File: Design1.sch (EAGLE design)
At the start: 24 parts, among them U1 ATMEGA328P-AU, X1 +3.3

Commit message: update
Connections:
- net ESP12F(PIN21) renamed RX
- net ESP12F(PIN22) renamed TX
- net N$5 renamed CH_PD
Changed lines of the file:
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@@
 <?xml version="1.0" encoding="utf-8"?>
 <!DOCTYPE eagle SYSTEM "eagle.dtd">
-<eagle version="8.5.2">
+<eagle version="8.7.1">
 <drawing>
 <settings>
@@
 </segment>
 </net>
-<net name="ESP12F(PIN21)" class="0">
+<net name="RX" class="0">
 <segment>
 <pinref part="SJ2" gate="1" pin="1"/>
@@
 <pinref part="U1" gate="A" pin="PD1"/>
 <wire x1="342.9" y1="220.98" x2="302.26" y2="220.98" width="0.1524" layer="91"/>
-</segment>
-</net>
-<net name="ESP12F(PIN22)" class="0">
+<label x="358.14" y="167.64" size="1.778" layer="95"/>
+</segment>
+</net>
+<net name="TX" class="0">
 <segment>
 <wire x1="340.36" y1="238.76" x2="340.36" y2="223.52" width="0.1524" layer="91"/>
@@
 <pinref part="MCU_FIRM2" gate="FIRM_PADS" pin="3"/>
 <wire x1="345.44" y1="170.18" x2="342.9" y2="170.18" width="0.1524" layer="91"/>
+<label x="347.98" y="170.18" size="1.778" layer="95"/>
 </segment>
 </net>
@@
 </segment>
 </net>
-<net name="N$5" class="0">
+<net name="CH_PD" class="0">
 <segment>
 <pinref part="U2" gate="G$1" pin="CH_PD"/>
 <wire x1="391.16" y1="233.68" x2="388.62" y2="233.68" width="0.1524" layer="91"/>
-<wire x1="401.32" y1="236.22" x2="391.16" y2="236.22" width="0.1524" layer="91"/>
-<wire x1="391.16" y1="236.22" x2="391.16" y2="233.68" width="0.1524" layer="91"/>
-</segment>
-</net>
+<label x="393.7" y="233.68" size="1.778" layer="95"/>
+</segment>
+</net>

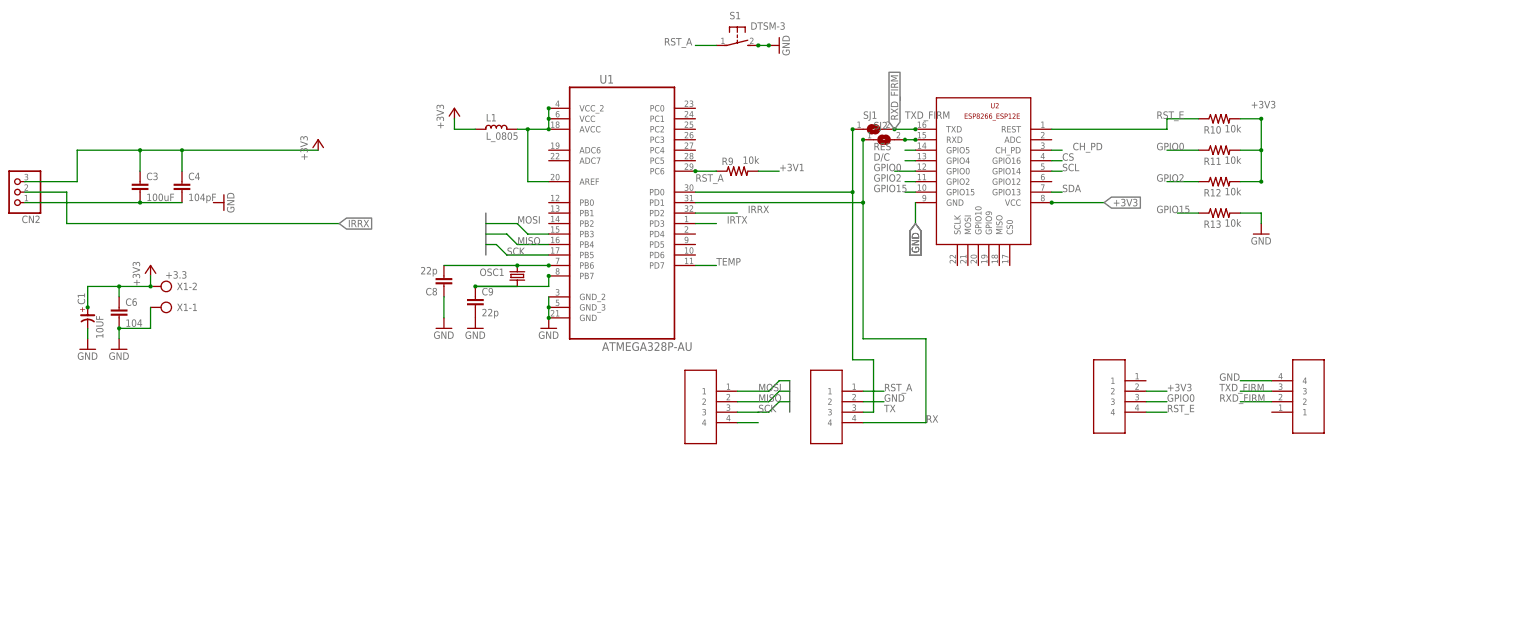
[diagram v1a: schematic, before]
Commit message: v 0.3 needs location buttons only
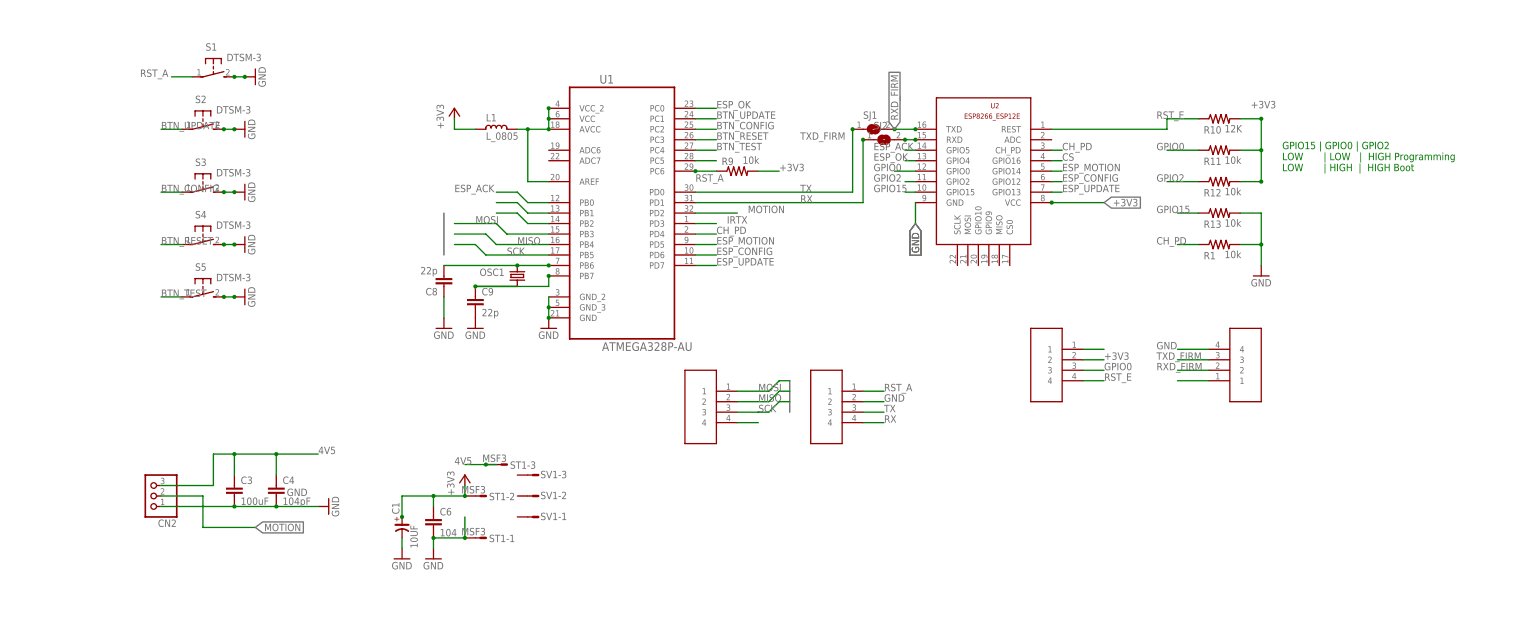
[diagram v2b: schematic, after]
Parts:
- removed X1: +3.3, con-ptr500:AK300/2
- added R1: 10k, SMD Resistors:0.75OHM-1/4W-1%(0805)
- added S2, S3, S4, S5: DTSM-3, switch-tact:DTSM-3
- added ST1: MSF3, con-lumberg:MSF3
- added SV1: (no value), con-amp-mt6:MT6-3Y
- R10: value 10k -> 12K
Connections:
- net IRRX renamed MOTION
- removed net +3V1: R9.2
- removed net D/C: U2.GPIO4
- removed net N$2: C3.2, C4.2, CN2.1
- removed net RES: U2.GPIO5
- removed net SCL: U2.GPIO14
- removed net SDA: U2.GPIO13
- removed net TEMP: U1.PD7
- new net 4V5: C3.1, C4.1, CN2.3, ST1-3.S
- new net BTN_CONFIG: S3.1, U1.PC2
- new net BTN_RESET: S4.1, U1.PC3
- new net BTN_TEST: S5.1, U1.PC4
- new net BTN_UPDATE: S2.1, U1.PC1
- new net ESP_ACK: U1.PB0, U2.GPIO5
- new net ESP_CONFIG: U1.PD6, U2.GPIO12
- new net ESP_MOTION: U1.PD5, U2.GPIO14
- new net ESP_OK: U1.PC0, U2.GPIO4
- new net ESP_UPDATE: U1.PD7, U2.GPIO13
- new net N$1: MCU_FIRM3.1
- new net N$18: U1.PC5
- new net N$4: U$3.1
- new net N$8: U1.PB1
- new net N$9: U1.PB2
- net +3V3: now also R9.2, ST1-2.S; no longer C3.1, C4.1, CN2.3, X1-2.KL
- net CH_PD: now also R1.1, U1.PD4
- net GND: now also C3.2, C4.2, CN2.1, R1.2, S2.2, S3.2, S4.2, S5.2, ST1-1.S; no longer X1-1.KL
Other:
- note added: "GPIO15 | GPIO0 | GPIO2 LOW | LOW | HIGH Programming LOW | HIGH | HIGH Boot"
- moved on the sheet: C1, C3, C4, C6, CN2, S1

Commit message: v 0.5 good
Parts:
- CON1: value FIRM_PADSSMD_FIRM_PADS -> AT1
- CON2: value FIRM_PADSSMD_FIRM_PADS -> AT2
- CON3: value FIRM_PADSSMD_FIRM_PADS -> ESP1
- CON4: value FIRM_PADSSMD_FIRM_PADS -> ESP2
- S1: value DTSM-3 -> RESET_A
- S2: value DTSM-3 -> UPDATE
- S3: value DTSM-3 -> CONFIG
- S4: value DTSM-3 -> RESET
- S5: value DTSM-3 -> TEST
- renumbered MCU_FIRM1 to CON1, MCU_FIRM2 to CON2, MCU_FIRM3 to CON3, U$3 to CON4
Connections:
- net N$11 renamed AT_VCC
- removed net N$1: CON3.1
- removed net N$17: CON1.4
- net CH_PD: now also CON3.1
- net GND: now also CON1.4; no longer CON2.2
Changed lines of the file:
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@@
 <?xml version="1.0" encoding="utf-8"?>
 <!DOCTYPE eagle SYSTEM "eagle.dtd">
-<eagle version="8.5.2">
+<eagle version="8.7.1">
 <drawing>
 <settings>
@@
 <part name="SJ2" library="jumper" deviceset="SJ" device=""/>
 <part name="GND5" library="supply1" deviceset="GND" device=""/>
-<part name="S1" library="switch-tact" deviceset="DTSM-3" device=""/>
+<part name="S1" library="switch-tact" deviceset="DTSM-3" device="" value="RESET_A"/>
 <part name="GND6" library="supply1" deviceset="GND" device=""/>
 <part name="R10" library="SMD Resistors" deviceset="0.75OHM-1/4W-1%(0805)" device="" value="12K"/>
@@
 <part name="GND7" library="supply1" deviceset="GND" device=""/>
 <part name="GND12" library="supply1" deviceset="GND" device=""/>
-<part name="MCU_FIRM1" library="firm_pads" deviceset="FIRM_PADS" device="SMD_FIRM_PADS"/>
-<part name="MCU_FIRM2" library="firm_pads" deviceset="FIRM_PADS" device="SMD_FIRM_PADS"/>
-<part name="U$3" library="firm_pads" deviceset="FIRM_PADS" device="SMD_FIRM_PADS"/>
-<part name="MCU_FIRM3" library="firm_pads" deviceset="FIRM_PADS" device="SMD_FIRM_PADS"/>
+<part name="CON1" library="firm_pads" deviceset="FIRM_PADS" device="SMD_FIRM_PADS" value="AT1"/>
+<part name="CON2" library="firm_pads" deviceset="FIRM_PADS" device="SMD_FIRM_PADS" value="AT2"/>
+<part name="CON4" library="firm_pads" deviceset="FIRM_PADS" device="SMD_FIRM_PADS" value="ESP2"/>
+<part name="CON3" library="firm_pads" deviceset="FIRM_PADS" device="SMD_FIRM_PADS" value="ESP1"/>
 <part name="GND10" library="supply1" deviceset="GND" device=""/>
 <part name="+3V1" library="supply1" deviceset="+3V3" device=""/>
@@
 <part name="SV1" library="con-amp-mt6" library_urn="urn:adsk.eagle:library:124" deviceset="MT6-3Y" device="" package3d_urn="urn:adsk.eagle:package:5892/1"/>
 <part name="ST1" library="con-lumberg" library_urn="urn:adsk.eagle:library:163" deviceset="MSF3" device="" package3d_urn="urn:adsk.eagle:package:8526/1"/>
-<part name="S2" library="switch-tact" deviceset="DTSM-3" device=""/>
+<part name="S2" library="switch-tact" deviceset="DTSM-3" device="" value="UPDATE"/>
 <part name="GND3" library="supply1" deviceset="GND" device=""/>
-<part name="S3" library="switch-tact" deviceset="DTSM-3" device=""/>
+<part name="S3" library="switch-tact" deviceset="DTSM-3" device="" value="CONFIG"/>
 <part name="GND8" library="supply1" deviceset="GND" device=""/>
-<part name="S4" library="switch-tact" deviceset="DTSM-3" device=""/>
+<part name="S4" library="switch-tact" deviceset="DTSM-3" device="" value="RESET"/>
 <part name="GND9" library="supply1" deviceset="GND" device=""/>
-<part name="S5" library="switch-tact" deviceset="DTSM-3" device=""/>
+<part name="S5" library="switch-tact" deviceset="DTSM-3" device="" value="TEST"/>
 <part name="GND11" library="supply1" deviceset="GND" device=""/>
 </parts>
@@
 <instance part="GND7" gate="1" x="238.76" y="134.62"/>
 <instance part="GND12" gate="1" x="213.36" y="147.32" rot="R90"/>
-<instance part="MCU_FIRM1" gate="FIRM_PADS" x="309.88" y="165.1"/>
-<instance part="MCU_FIRM2" gate="FIRM_PADS" x="340.36" y="165.1"/>
-<instance part="U$3" gate="FIRM_PADS" x="429.26" y="187.96" rot="R180"/>
-<instance part="MCU_FIRM3" gate="FIRM_PADS" x="393.7" y="175.26"/>
+<instance part="CON1" gate="FIRM_PADS" x="309.88" y="165.1"/>
+<instance part="CON2" gate="FIRM_PADS" x="340.36" y="165.1"/>
+<instance part="CON4" gate="FIRM_PADS" x="429.26" y="187.96" rot="R180"/>
+<instance part="CON3" gate="FIRM_PADS" x="393.7" y="175.26"/>
 <instance part="GND10" gate="1" x="231.14" y="134.62"/>
 <instance part="+3V1" gate="G$1" x="246.38" y="154.94"/>
@@
 </segment>
 <segment>
-<pinref part="MCU_FIRM2" gate="FIRM_PADS" pin="2"/>
-<wire x1="342.9" y1="172.72" x2="347.98" y2="172.72" width="0.1524" layer="91"/>
-<label x="347.98" y="172.72" size="1.778" layer="95"/>
-</segment>
-<segment>
-<pinref part="U$3" gate="FIRM_PADS" pin="4"/>
+<pinref part="CON4" gate="FIRM_PADS" pin="4"/>
 <wire x1="426.72" y1="185.42" x2="419.1" y2="185.42" width="0.1524" layer="91"/>
 <label x="414.02" y="185.42" size="1.778" layer="95"/>
@@
 <junction x="190.5" y="198.12"/>
 </segment>
+<segment>
+<pinref part="CON1" gate="FIRM_PADS" pin="4"/>
+<wire x1="312.42" y1="167.64" x2="317.5" y2="167.64" width="0.1524" layer="91"/>
+<label x="317.5" y="167.64" size="1.778" layer="95"/>
+</segment>
 </net>
 <net name="RX" class="0">
@@
 </segment>
 <segment>
-<pinref part="MCU_FIRM2" gate="FIRM_PADS" pin="4"/>
+<pinref part="CON2" gate="FIRM_PADS" pin="4"/>
 <wire x1="342.9" y1="167.64" x2="347.98" y2="167.64" width="0.1524" layer="91"/>
 <label x="347.98" y="167.64" size="1.778" layer="95"/>
@@
 </segment>
 <segment>
-<pinref part="MCU_FIRM2" gate="FIRM_PADS" pin="3"/>
+<pinref part="CON2" gate="FIRM_PADS" pin="3"/>
 <wire x1="347.98" y1="170.18" x2="342.9" y2="170.18" width="0.1524" layer="91"/>
 <label x="347.98" y="170.18" size="1.778" layer="95"/>
@@
 </segment>
 <segment>
-<pinref part="U$3" gate="FIRM_PADS" pin="3"/>
+<pinref part="CON4" gate="FIRM_PADS" pin="3"/>
 <wire x1="426.72" y1="182.88" x2="419.1" y2="182.88" width="0.1524" layer="91"/>
 <label x="414.02" y="182.88" size="1.778" layer="95"/>
@@
 <wire x1="325.12" y1="175.26" x2="322.58" y2="175.26" width="0.1524" layer="91"/>
 <wire x1="322.58" y1="175.26" x2="320.04" y2="172.72" width="0.1524" layer="91"/>
-<pinref part="MCU_FIRM1" gate="FIRM_PADS" pin="2"/>
+<pinref part="CON1" gate="FIRM_PADS" pin="2"/>
 <wire x1="312.42" y1="172.72" x2="320.04" y2="172.72" width="0.1524" layer="91"/>
 <label x="317.5" y="172.72" size="1.778" layer="95"/>
@@
 <net name="SCK" class="0">
 <segment>
-<pinref part="MCU_FIRM1" gate="FIRM_PADS" pin="3"/>
+<pinref part="CON1" gate="FIRM_PADS" pin="3"/>
 <wire x1="312.42" y1="170.18" x2="317.5" y2="170.18" width="0.1524" layer="91"/>
 <label x="317.5" y="170.18" size="1.778" layer="95"/>
@@
 <wire x1="325.12" y1="177.8" x2="322.58" y2="177.8" width="0.1524" layer="91"/>
 <wire x1="322.58" y1="177.8" x2="320.04" y2="175.26" width="0.1524" layer="91"/>
-<pinref part="MCU_FIRM1" gate="FIRM_PADS" pin="1"/>
+<pinref part="CON1" gate="FIRM_PADS" pin="1"/>
 <wire x1="312.42" y1="175.26" x2="320.04" y2="175.26" width="0.1524" layer="91"/>
 <label x="317.5" y="175.26" size="1.778" layer="95"/>
@@
 </segment>
 <segment>
-<pinref part="U$3" gate="FIRM_PADS" pin="2"/>
+<pinref part="CON4" gate="FIRM_PADS" pin="2"/>
 <wire x1="426.72" y1="180.34" x2="419.1" y2="180.34" width="0.1524" layer="91"/>
 <label x="414.02" y="180.34" size="1.778" layer="95"/>
 </segment>
 </net>
-<net name="N$11" class="1">
+<net name="AT_VCC" class="1">
 <segment>
 <pinref part="U1" gate="A" pin="AVCC"/>
@@
 <wire x1="261.62" y1="226.06" x2="261.62" y2="238.76" width="0.1524" layer="91"/>
 <junction x="261.62" y="238.76"/>
+<label x="256.54" y="241.3" size="1.778" layer="95"/>
 </segment>
 </net>
@@
 </segment>
 <segment>
-<pinref part="MCU_FIRM3" gate="FIRM_PADS" pin="4"/>
+<pinref part="CON3" gate="FIRM_PADS" pin="4"/>
 <wire x1="396.24" y1="177.8" x2="401.32" y2="177.8" width="0.1524" layer="91"/>
 <label x="401.32" y="177.8" size="1.778" layer="95"/>
@@
 </segment>
 <segment>
-<pinref part="MCU_FIRM3" gate="FIRM_PADS" pin="3"/>
+<pinref part="CON3" gate="FIRM_PADS" pin="3"/>
 <wire x1="396.24" y1="180.34" x2="401.32" y2="180.34" width="0.1524" layer="91"/>
 <label x="401.32" y="180.34" size="1.778" layer="95"/>
@@
 </segment>
 <segment>
-<pinref part="MCU_FIRM2" gate="FIRM_PADS" pin="1"/>
+<pinref part="CON2" gate="FIRM_PADS" pin="1"/>
 <wire x1="342.9" y1="175.26" x2="347.98" y2="175.26" width="0.1524" layer="91"/>
 <label x="347.98" y="175.26" size="1.778" layer="95"/>
@@
 <wire x1="302.26" y1="243.84" x2="307.34" y2="243.84" width="0.1524" layer="91"/>
 <label x="307.34" y="243.84" size="1.778" layer="95"/>
-</segment>
-</net>
-<net name="N$17" class="0">
-<segment>
-<pinref part="MCU_FIRM1" gate="FIRM_PADS" pin="4"/>
-<wire x1="312.42" y1="167.64" x2="317.5" y2="167.64" width="0.1524" layer="91"/>
 </segment>
 </net>
@@
 </segment>
 <segment>
-<pinref part="MCU_FIRM3" gate="FIRM_PADS" pin="2"/>
+<pinref part="CON3" gate="FIRM_PADS" pin="2"/>
 <wire x1="396.24" y1="182.88" x2="401.32" y2="182.88" width="0.1524" layer="91"/>
 <label x="401.32" y="182.88" size="1.778" layer="95"/>
@@
 <label x="307.34" y="213.36" size="1.778" layer="95"/>
 </segment>
+<segment>
+<pinref part="CON3" gate="FIRM_PADS" pin="1"/>
+<wire x1="396.24" y1="185.42" x2="401.32" y2="185.42" width="0.1524" layer="91"/>
+<label x="401.32" y="185.42" size="1.778" layer="95"/>
+</segment>
 </net>
 <net name="ESP_CONFIG" class="0">
@@
 </segment>
 </net>
-<net name="N$1" class="0">
-<segment>
-<pinref part="MCU_FIRM3" gate="FIRM_PADS" pin="1"/>
-<wire x1="396.24" y1="185.42" x2="401.32" y2="185.42" width="0.1524" layer="91"/>
-</segment>
-</net>
 <net name="N$4" class="0">
 <segment>
-<pinref part="U$3" gate="FIRM_PADS" pin="1"/>
+<pinref part="CON4" gate="FIRM_PADS" pin="1"/>
 <wire x1="426.72" y1="177.8" x2="419.1" y2="177.8" width="0.1524" layer="91"/>
 </segment>

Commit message: v0.6
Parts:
- removed SV1: (no value), con-amp-mt6:MT6-3Y
- added BAT: Bat, jumper:SJ
- added BATL3.3: 3.3, jumper:SJ
- added BATL4.5: 4.5, jumper:SJ
- added CN1: (no value), MicroUSB:USB""
- added SG1: F/CM12P, buzzer:F/CM12P
- added U3: LDO, SPX3819M5-L-3-3:SPX3819M5-L-3-3
- S1, S2, S3, S4, S5: device switch-tact:DTSM-3 -> switch-tact:DTSM-6
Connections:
- net N$9 renamed SS-
- removed net N$8: U1.PB1
- new net BAT: BAT.2, BATL3.3.1, ST1-2.S
- new net BUZZER: SG1.1, U1.PB1
- new net N$1: BATL3.3.2, BATL4.5.2, CN1.VBUS, U3.EN, U3.VIN
- net +3V3: now also BAT.1, U3.VOUT; no longer ST1-2.S
- net 4V5: now also BATL4.5.1
- net GND: now also CN1.GND, S1.3, S2.3, S3.3, S4.3, S5.3, SG1.2, U3.GND; no longer S1.2, S2.2, S3.2, S4.2, S5.2
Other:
- moved on the sheet: C1, C3, C4, C6, CN2, ST1-1, ST1-2, ST1-3
